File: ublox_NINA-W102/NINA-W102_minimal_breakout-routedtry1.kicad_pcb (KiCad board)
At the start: 2 copper layers, 16 parts, among them J1 Conn_01x15, J2 Conn_01x15, J3 6_PIN_SERIAL_TARGETLOCK, SW1 BOOT, SW2 RESET, U1 NINA-W102

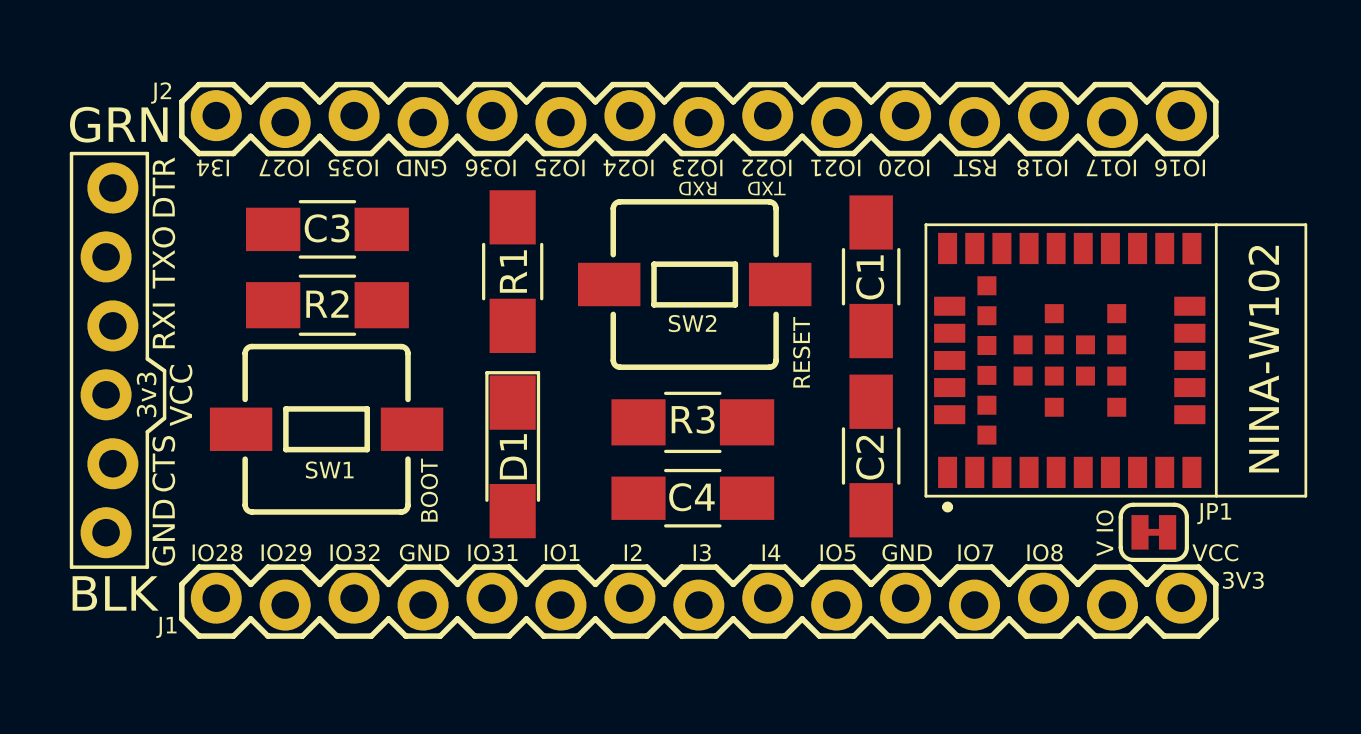
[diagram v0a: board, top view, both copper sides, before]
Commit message: initial layout done without wiring
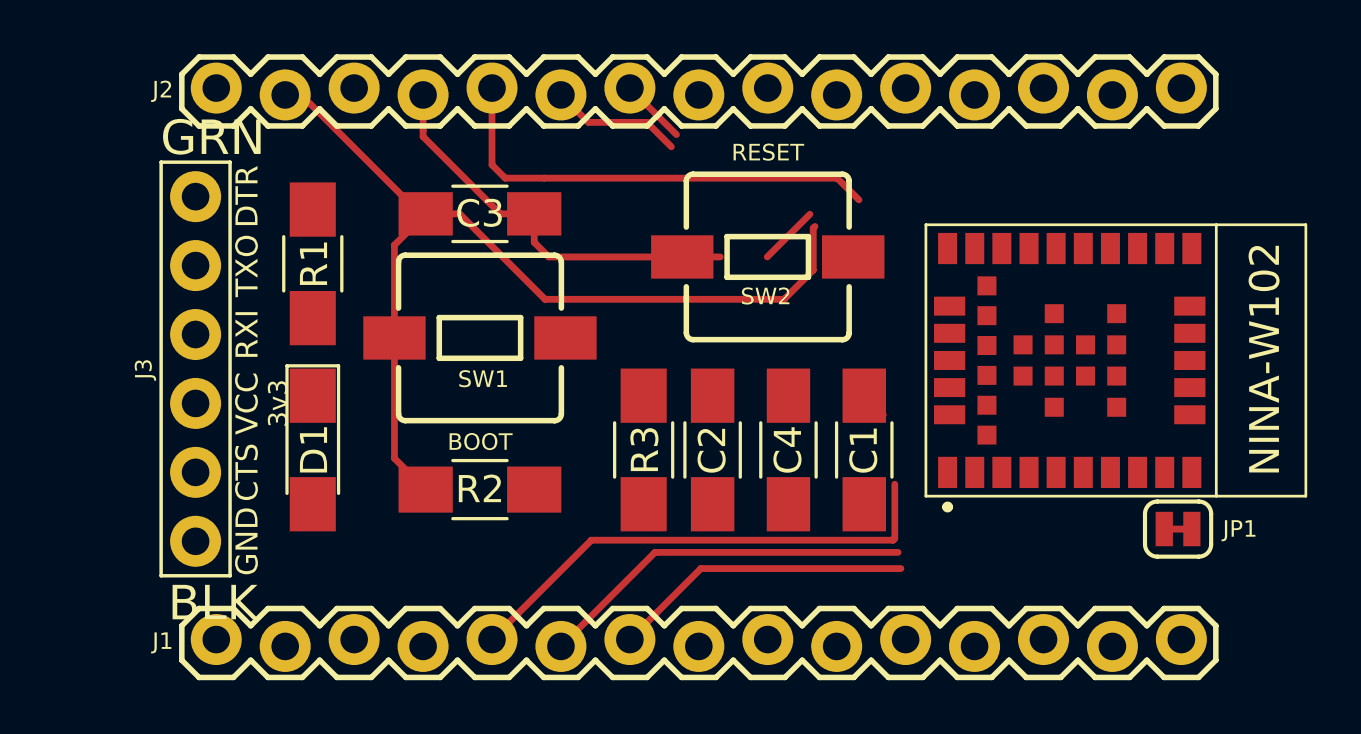
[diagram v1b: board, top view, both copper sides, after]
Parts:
- removed ?: , lib:BREADBOARD_SPACING_80mm
- J3: footprint 6_PIN_SERIAL_TARGET_SIDE_W_SILK -> lib:6_PIN_SERIAL_TARGET_SIDE_W_SILK
- moved R2 8.82 mm to (120.2, 111.2)
- moved R1 7.37 mm to (114.0, 102.9)
- moved D1 7.37 mm to (114.0, 109.7)
- moved SW1 6.58 mm to (120.2, 105.6)
- moved C1 6.39 mm to (134.4, 109.7)
- moved C3 5.65 mm to (120.2, 101.0)
- moved J3 3.06 mm to (109.7, 106.7)
- moved C2 3.06 mm to (131.6, 109.7)
- moved SW2 2.88 mm to (130.8, 102.6)
- moved R3 2.08 mm to (126.2, 109.7), turned to 90 degrees
- moved C4 1.92 mm to (128.8, 109.7), turned to 270 degrees
- moved J1 1.52 mm to (110.5, 116.8)
- moved J2 1.02 mm to (110.5, 96.5)
- moved JP1 0.90 mm to (145.9, 112.6)
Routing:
- net CTS: track 0.00 -> 35.8 mm
- net Net-(J1-Pad5): track 0.00 -> 18.4 mm
- net GND: track 0.00 -> 18.2 mm
- net Net-(J2-Pad5): track 0.00 -> 16.9 mm
- net Net-(J1-Pad6): track 0.00 -> 13.9 mm
- net Net-(J1-Pad7): track 0.00 -> 11.1 mm
- net Net-(J2-Pad6): track 0.00 -> 4.86 mm
- net Net-(J2-Pad7): track 0.00 -> 2.43 mm
- net DTR: track 0.00 -> 0.81 mm
- net Net-(J2-Pad15): track 0.00 -> 0.55 mm
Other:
- net class power removed
- rule via_min_drill: 0.3302 -> 0.254
- rule via_min_size: 0.6858 -> 0.508
- board text removed: "3V3"
- board text removed: "GND"
- board text removed: "I2"
- board text removed: "I3"
- board text removed: "I34"
- board text removed: "I4"
- board text removed: "IO1"
- board text removed: "IO16"
- board text removed: "IO17"
- board text removed: "IO18"
- board text removed: "IO20"
- board text removed: "IO21"
- board text removed: "IO22"
- board text removed: "IO23"
- board text removed: "IO24"
- board text removed: "IO25"
- board text removed: "IO27"
- board text removed: "IO28"
- board text removed: "IO29"
- board text removed: "IO31"
- board text removed: "IO32"
- board text removed: "IO35"
- board text removed: "IO36"
- board text removed: "IO5"
- board text removed: "IO7"
- board text removed: "IO8"
- board text removed: "RST"
- board text removed: "RXD"
- board text removed: "TXD"
- board text removed: "V IO"
- board text removed: "VCC"
